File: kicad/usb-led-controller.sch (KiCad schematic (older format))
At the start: 45 parts, among them J1 SWD, J2 PWR, J3 USB, J4 PWM_0, J5 PWM_1, J6 WS2812_0, J7 WS2812_1, Q1 NVS4409N, Q2 NVS4409N, Q3 NVS4409N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

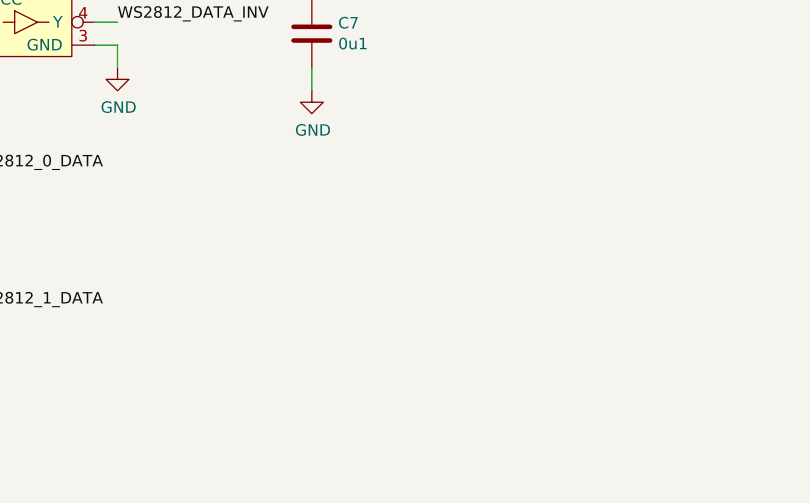
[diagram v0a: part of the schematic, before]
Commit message: Added some pullups
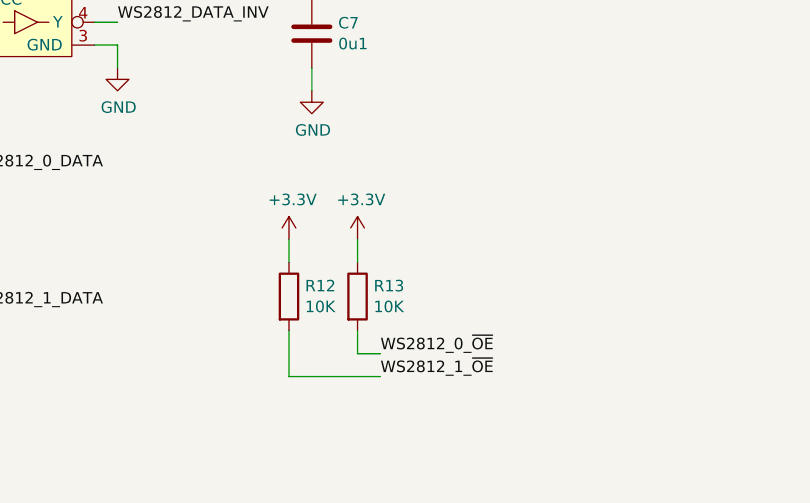
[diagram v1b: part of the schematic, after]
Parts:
- added R12, R13: 10K, Resistor_SMD:R_0402_1005Metric, symbol Device:R
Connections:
- net +3V3: now also R12.1, R13.1
- net WS2812_0_~OE: now also R13.2
- net WS2812_1_~OE: now also R12.2
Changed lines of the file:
@@
 	0    1    1    0
 $EndComp
+$Comp
+L Device:R R12
+U 1 1 5FC2AA22
+P 5950 6950
+F 0 "R12" H 6020 6996 50  0000 L CNN
+F 1 "10K" H 6020 6905 50  0000 L CNN
+F 2 "Resistor_SMD:R_0402_1005Metric" V 5880 6950 50  0001 C CNN
+F 3 "~" H 5950 6950 50  0001 C CNN
+	1    5950 6950
+	1    0    0    -1
+$EndComp
+$Comp
+L Device:R R13
+U 1 1 5FC2B0C0
+P 6250 6950
+F 0 "R13" H 6320 6996 50  0000 L CNN
+F 1 "10K" H 6320 6905 50  0000 L CNN
+F 2 "Resistor_SMD:R_0402_1005Metric" V 6180 6950 50  0001 C CNN
+F 3 "~" H 6250 6950 50  0001 C CNN
+	1    6250 6950
+	1    0    0    -1
+$EndComp
+$Comp
+L power:+3.3V #PWR02
+U 1 1 5FC2BA79
+P 5950 6700
+F 0 "#PWR02" H 5950 6550 50  0001 C CNN
+F 1 "+3.3V" H 5965 6873 50  0000 C CNN
+F 2 "" H 5950 6700 50  0001 C CNN
+F 3 "" H 5950 6700 50  0001 C CNN
+	1    5950 6700
+	1    0    0    -1
+$EndComp
+$Comp
+L power:+3.3V #PWR03
+U 1 1 5FC2C655
+P 6250 6700
+F 0 "#PWR03" H 6250 6550 50  0001 C CNN
+F 1 "+3.3V" H 6265 6873 50  0000 C CNN
+F 2 "" H 6250 6700 50  0001 C CNN
+F 3 "" H 6250 6700 50  0001 C CNN
+	1    6250 6700
+	1    0    0    -1
+$EndComp
+Text Label 6350 7200 0    50   ~ 0
+WS2812_0_~OE
+Wire Wire Line
+	6350 7200 6250 7200
+Wire Wire Line
+	6250 7200 6250 7100
+Text Label 6350 7300 0    50   ~ 0
+WS2812_1_~OE
+Wire Wire Line
+	6350 7300 5950 7300
+Wire Wire Line
+	5950 7300 5950 7100
+Wire Wire Line
+	5950 6800 5950 6700
+Wire Wire Line
+	6250 6700 6250 6800
 $EndSCHEMATC

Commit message: Updated part numbers on schematic for building
This doesn't belong on this branch..
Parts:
- J1: Part Number (none) -> 455-1790-1-ND
- J2: Part Number (none) -> 952-3233-ND
- J6, J7: Part Number (none) -> 952-3232-ND
- R1, R3, R5: Part Number (none) -> CR0402-J/-000GLFTR-ND
- R10, R11, R12, R13: Part Number (none) -> CR0402-JW-103GLFTR-ND
- R2: Part Number (none) -> CR0402-FX-1001GLFTR-ND
- R6, R7, R8, R9: Part Number (none) -> CR0402-JW-330GLFTR-ND
- U6: Part Number (none) -> 296-11600-2-ND
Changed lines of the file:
@@
 F 1 "SWD" H 718 2566 50  0000 C CNN
 F 2 "usb-led-controller:JST-SH-4" H 800 2900 50  0001 C CNN
-F 3 "455-1790-1-ND" H 800 2900 50  0001 C CNN
+F 3 "~" H 800 2900 50  0001 C CNN
+F 4 "455-1790-1-ND" H 800 2900 50  0001 C CNN "Part Number"
 	1    800  2900
 	-1   0    0    1
@@
 F 2 "Resistor_SMD:R_0402_1005Metric" V 4530 4450 50  0001 C CNN
 F 3 "~" H 4600 4450 50  0001 C CNN
+F 4 "CR0402-JW-330GLFTR-ND" H 4600 4450 50  0001 C CNN "Part Number"
 	1    4600 4450
 	0    1    1    0
@@
 F 2 "Resistor_SMD:R_0402_1005Metric" V 4530 4750 50  0001 C CNN
 F 3 "~" H 4600 4750 50  0001 C CNN
+F 4 "CR0402-JW-330GLFTR-ND" H 4600 4750 50  0001 C CNN "Part Number"
 	1    4600 4750
 	0    1    1    0
@@
 F 2 "Resistor_SMD:R_0402_1005Metric" V 3580 1200 50  0001 C CNN
 F 3 "~" H 3650 1200 50  0001 C CNN
+F 4 "CR0402-FX-1001GLFTR-ND" H 3650 1200 50  0001 C CNN "Part Number"
 	1    3650 1200
 	1    0    0    -1
@@
 F 2 "Resistor_SMD:R_0402_1005Metric" V 4180 1150 50  0001 C CNN
 F 3 "~" H 4250 1150 50  0001 C CNN
+F 4 "CR0402-J/-000GLFTR-ND" H 4250 1150 50  0001 C CNN "Part Number"
 	1    4250 1150
 	0    1    1    0
@@
 F 2 "Resistor_SMD:R_0402_1005Metric" V 730 3700 50  0001 C CNN
 F 3 "~" H 800 3700 50  0001 C CNN
+F 4 "CR0402-J/-000GLFTR-ND" H 800 3700 50  0001 C CNN "Part Number"
 	1    800  3700
 	1    0    0    -1
@@
 F 2 "usb-led-controller:M20-88904" H 800 5300 50  0001 C CNN
 F 3 "~" H 800 5300 50  0001 C CNN
+F 4 "952-3233-ND" H 800 5300 50  0001 C CNN "Part Number"
 	1    800  5300
 	-1   0    0    -1
@@
 F 2 "usb-led-controller:M20-88903" H 10450 2950 50  0001 C CNN
 F 3 "~" H 10450 2950 50  0001 C CNN
+F 4 "952-3232-ND" H 10450 2950 50  0001 C CNN "Part Number"
 	1    10450 2950
 	1    0    0    -1
@@
 F 2 "Resistor_SMD:R_0402_1005Metric" V 3730 6400 50  0001 C CNN
 F 3 "~" H 3800 6400 50  0001 C CNN
+F 4 "CR0402-JW-330GLFTR-ND" H 3800 6400 50  0001 C CNN "Part Number"
 	1    3800 6400
 	0    1    1    0
@@
 F 2 "Resistor_SMD:R_0402_1005Metric" V 3730 7000 50  0001 C CNN
 F 3 "~" H 3800 7000 50  0001 C CNN
+F 4 "CR0402-JW-330GLFTR-ND" H 3800 7000 50  0001 C CNN "Part Number"
 	1    3800 7000
 	0    1    1    0
@@
 F 2 "Resistor_SMD:R_0402_1005Metric" V 3880 5050 50  0001 C CNN
 F 3 "~" H 3950 5050 50  0001 C CNN
+F 4 "CR0402-J/-000GLFTR-ND" H 3950 5050 50  0001 C CNN "Part Number"
 	1    3950 5050
 	1    0    0    -1
@@
 F 2 "usb-led-controller:M20-88903" H 10450 3350 50  0001 C CNN
 F 3 "~" H 10450 3350 50  0001 C CNN
+F 4 "952-3232-ND" H 10450 3350 50  0001 C CNN "Part Number"
 	1    10450 3350
 	1    0    0    -1
@@
 F 2 "Package_TO_SOT_SMD:SOT-353_SC-70-5" H 4800 5750 50  0001 C CNN
 F 3 "" H 4800 5750 50  0001 C CNN
+F 4 "296-11600-2-ND" H 4800 5750 50  0001 C CNN "Part Number"
 	1    4800 5750
 	1    0    0    -1
@@
 F 2 "Resistor_SMD:R_0402_1005Metric" V 4230 7300 50  0001 C CNN
 F 3 "~" H 4300 7300 50  0001 C CNN
+F 4 "CR0402-JW-103GLFTR-ND" H 4300 7300 50  0001 C CNN "Part Number"
 	1    4300 7300
 	1    0    0    -1
@@
 F 2 "Resistor_SMD:R_0402_1005Metric" V 3980 6650 50  0001 C CNN
 F 3 "~" H 4050 6650 50  0001 C CNN
+F 4 "CR0402-JW-103GLFTR-ND" H 4050 6650 50  0001 C CNN "Part Number"
 	1    4050 6650
 	1    0    0    -1
@@
 F 2 "Resistor_SMD:R_0402_1005Metric" V 5880 6950 50  0001 C CNN
 F 3 "~" H 5950 6950 50  0001 C CNN
+F 4 "CR0402-JW-103GLFTR-ND" H 5950 6950 50  0001 C CNN "Part Number"
 	1    5950 6950
 	1    0    0    -1
@@
 F 2 "Resistor_SMD:R_0402_1005Metric" V 6180 6950 50  0001 C CNN
 F 3 "~" H 6250 6950 50  0001 C CNN
+F 4 "CR0402-JW-103GLFTR-ND" H 6250 6950 50  0001 C CNN "Part Number"
 	1    6250 6950
 	1    0    0    -1

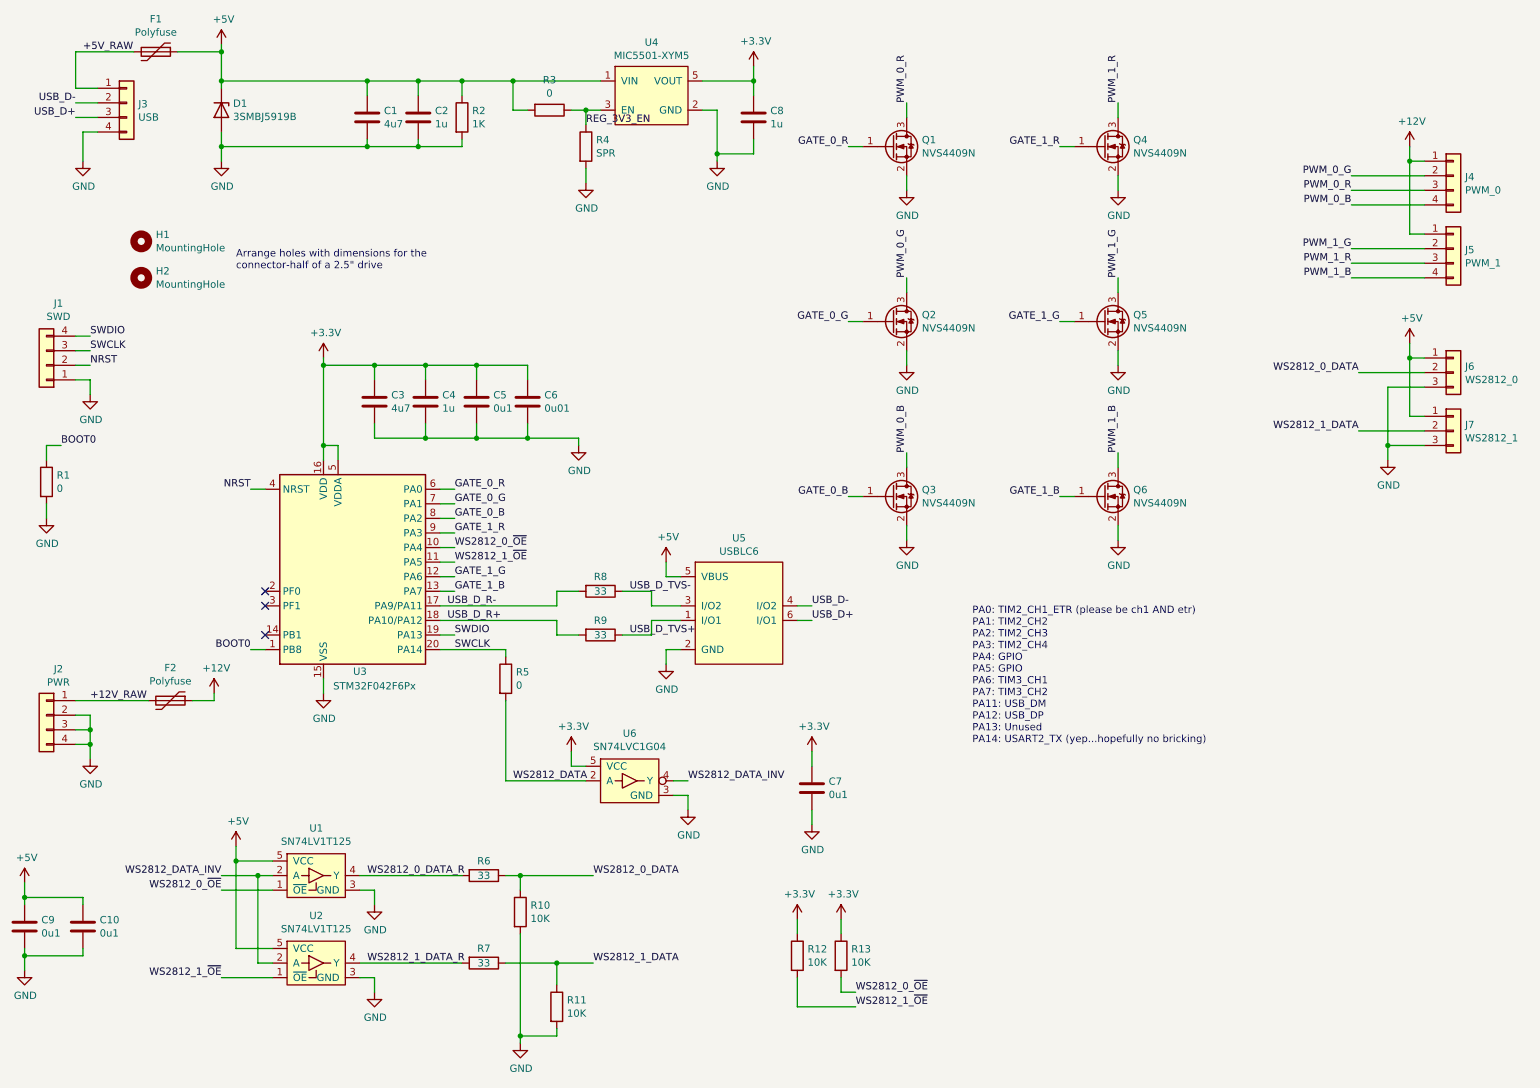
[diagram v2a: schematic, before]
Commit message: Updating schematic to use an EFM32HG microcontroller
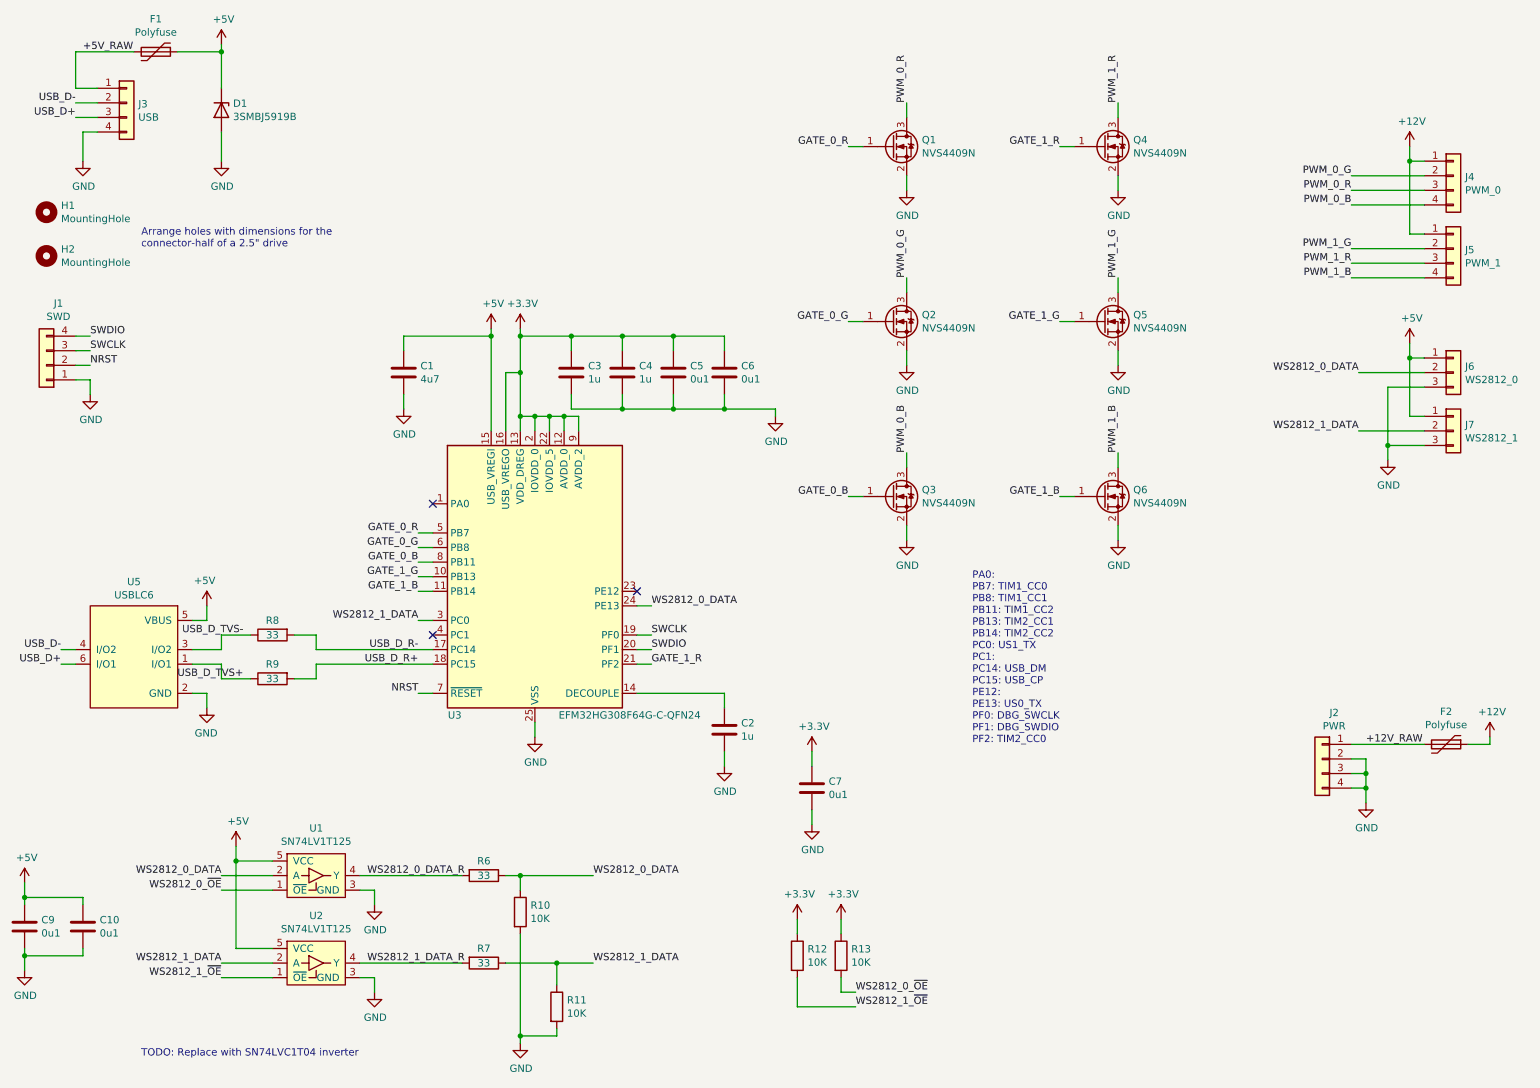
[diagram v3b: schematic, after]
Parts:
- removed C8: 1u, Capacitor_SMD:C_0603_1608Metric, symbol Device:C
- removed R1, R3, R5: 0, Resistor_SMD:R_0402_1005Metric, symbol Device:R
- removed R2: 1K, Resistor_SMD:R_0402_1005Metric, symbol Device:R
- removed R4: SPR, Resistor_SMD:R_0402_1005Metric, symbol Device:R
- removed U3: STM32F042F6Px, Package_SO:TSSOP-20_4.4x6.5mm_P0.65mm, symbol MCU_ST_STM32F0:STM32F042F6Px
- removed U4: MIC5501-XYM5, Package_TO_SOT_SMD:SOT-23-5, symbol usb-led-controller:MIC5501-XYM5
- removed U6: SN74LVC1G04, Package_TO_SOT_SMD:SOT-353_SC-70-5, symbol usb-led-controller:SN74LVC1G04
- added U3: EFM32HG308F64G-C-QFN24, Package_DFN_QFN:QFN-24-1EP_5x5mm_P0.65mm_EP3.6x3.6mm, symbol MCU_SiliconLabs:EFM32HG308F64G-C-QFN24
- C3: value 4u7 -> 1u; Part Number 1276-1044-2-ND -> 1276-1102-2-ND
- C6: value 0u01 -> 0u1; Part Number 587-5482-2-ND -> 1276-1043-2-ND
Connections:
- net +3V3: now also U3.12 (AVDD_0), U3.13 (VDD_DREG), U3.16 (USB_VREGO), U3.2 (IOVDD_0), U3.22 (IOVDD_5), U3.9 (AVDD_2)
- net +5V: now also U3.15 (USB_VREGI); no longer C2.1
- net GATE_0_B: now also U3.8 (PB11)
- net GATE_0_G: now also U3.6 (PB8)
- net GATE_0_R: now also U3.5 (PB7)
- net GATE_1_B: now also U3.11 (PB14)
- net GATE_1_G: now also U3.10 (PB13)
- net GATE_1_R: now also U3.21 (PF2)
- net GND: now also U3.25 (VSS)
- net NRST: now also U3.7 (~RESET)
- net SWCLK: now also U3.19 (PF0)
- net SWDIO: now also U3.20 (PF1)
- net USB_D_R+: now also U3.18 (PC15)
- net USB_D_R-: now also U3.17 (PC14)
- net WS2812_0_DATA: now also U1.2 (A), U3.24 (PE13)
- net WS2812_1_DATA: now also U2.2 (A), U3.3 (PC0)
- removed net WS2812_DATA_INV: U1.2 (A), U2.2 (A)
- new net: C2.1, U3.14 (DECOUPLE)
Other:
- note added: "PA0:\nPB7: TIM1_CC0\nPB8: TIM1_CC1\nPB11: TIM1_CC2\nPB13: TIM2_CC1\nPB14: TIM2_CC2\nPC0: US1_TX\nPC1:\nPC14: USB_DM\nPC15: USB_CP\nPE12:\nPE13: US0_TX\nPF0: DBG_SWCLK\nPF1: DBG_SWDIO\nPF2: TIM2_CC0"
- note added: "TODO: Replace with SN74LVC1T04 inverter"
- note removed: "PA0: TIM2_CH1_ETR (please be ch1 AND etr)\nPA1: TIM2_CH2\nPA2: TIM2_CH3\nPA3: TIM2_CH4\nPA4: GPIO\nPA5: GPIO\nPA6: TIM3_CH1\nPA7: TIM3_CH2\nPA11: USB_DM\nPA12: USB_DP\nPA13: Unused\nPA14: USART2_TX (yep...hopefully no bricking)"
- moved on the sheet: C1, C3, C4, C5, C6, F2, H1, H2, J2, R8, R9, U5

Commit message: Placed new microcontroller and rearranged capacitors
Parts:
- removed C7: 0u1, Capacitor_SMD:C_0402_1005Metric, symbol Device:C
- C4: value 1u -> 0u1; footprint Capacitor_SMD:C_0603_1608Metric -> Capacitor_SMD:C_0402_1005Metric; Part Number 1276-1102-2-ND -> 1276-1043-2-ND
- U3: footprint Package_DFN_QFN:QFN-24-1EP_5x5mm_P0.65mm_EP3.6x3.6mm -> Package_DFN_QFN:QFN-24-1EP_5x5mm_P0.65mm_EP3.6x3.6mm_ThermalVias
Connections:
- net WS2812_0_DATA: no longer U1.2 (A), U3.24 (PE13)
- net WS2812_0_~OE: now also U3.23 (PE12)
- net WS2812_1_DATA: no longer U2.2 (A), U3.3 (PC0)
- net WS2812_1_~OE: now also U3.4 (PC1)
- net UC_DECOUPLE: now reaches C2.1, U3.14 (DECOUPLE)
- new net WS2812_0_DATA_UC: U1.2 (A), U3.24 (PE13)
- new net WS2812_1_DATA_UC: U2.2 (A), U3.3 (PC0)
- no-connect marks 3 -> 1
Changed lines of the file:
@@
 P 4750 2950
 F 0 "C4" H 4865 2996 50  0000 L CNN
-F 1 "1u" H 4865 2905 50  0000 L CNN
-F 2 "Capacitor_SMD:C_0603_1608Metric" H 4788 2800 50  0001 C CNN
+F 1 "0u1" H 4865 2905 50  0000 L CNN
+F 2 "Capacitor_SMD:C_0402_1005Metric" H 4788 2800 50  0001 C CNN
 F 3 "~" H 4750 2950 50  0001 C CNN
-F 4 "1276-1102-2-ND" H 4750 2950 50  0001 C CNN "Part Number"
+F 4 "1276-1043-2-ND" H 4750 2950 50  0001 C CNN "Part Number"
 	1    4750 2950
 	1    0    0    -1
@@
 F 4 "1276-1043-2-ND" H 5450 2950 50  0001 C CNN "Part Number"
 	1    5450 2950
-	1    0    0    -1
-$EndComp
-$Comp
-L Device:C C7
-U 1 1 5FC0A218
-P 6050 5800
-F 0 "C7" H 6165 5846 50  0000 L CNN
-F 1 "0u1" H 6165 5755 50  0000 L CNN
-F 2 "Capacitor_SMD:C_0402_1005Metric" H 6088 5650 50  0001 C CNN
-F 3 "~" H 6050 5800 50  0001 C CNN
-F 4 "1276-1043-2-ND" H 6050 5800 50  0001 C CNN "Part Number"
-	1    6050 5800
 	1    0    0    -1
 $EndComp
@@
 	2950 6400 3650 6400
 Text Label 2000 6400 2    50   ~ 0
-WS2812_0_DATA
+WS2812_0_DATA_UC
 $Comp
 L Connector_Generic:Conn_01x04 J3
@@
 Wire Wire Line
 	650  6950 650  7050
-$Comp
-L power:+3.3V #PWR0133
-U 1 1 5FD00D52
-P 6050 5550
-F 0 "#PWR0133" H 6050 5400 50  0001 C CNN
-F 1 "+3.3V" H 6065 5723 50  0000 C CNN
-F 2 "" H 6050 5550 50  0001 C CNN
-F 3 "" H 6050 5550 50  0001 C CNN
-	1    6050 5550
-	1    0    0    -1
-$EndComp
-Wire Wire Line
-	6050 5550 6050 5650
-$Comp
-L power:GND #PWR0134
-U 1 1 5FD0A22D
-P 6050 6050
-F 0 "#PWR0134" H 6050 5800 50  0001 C CNN
-F 1 "GND" H 6055 5877 50  0000 C CNN
-F 2 "" H 6050 6050 50  0001 C CNN
-F 3 "" H 6050 6050 50  0001 C CNN
-	1    6050 6050
-	1    0    0    -1
-$EndComp
-Wire Wire Line
-	6050 6050 6050 5950
 $Comp
 L Device:R R11
@@
 F 0 "U3" H 3600 3400 50  0000 C CNN
 F 1 "EFM32HG308F64G-C-QFN24" H 4800 3400 50  0000 C CNN
-F 2 "Package_DFN_QFN:QFN-24-1EP_5x5mm_P0.65mm_EP3.6x3.6mm" H 4200 3400 50  0001 C CNN
+F 2 "Package_DFN_QFN:QFN-24-1EP_5x5mm_P0.65mm_EP3.6x3.6mm_ThermalVias" H 4200 3400 50  0001 C CNN
 F 3 "https://www.silabs.com/documents/public/data-sheets/efm32hg-datasheet.pdf" H 4200 3400 50  0001 C CNN
 	1    4150 4350
@@
 	2000 6400 2350 6400
 Text Label 2000 7000 2    50   ~ 0
-WS2812_1_DATA
+WS2812_1_DATA_UC
 Wire Wire Line
 	2000 7000 2350 7000
@@
 TODO: Replace with SN74LVC1T04 inverter
 Text Label 4950 4550 0    50   ~ 0
-WS2812_0_DATA
+WS2812_0_DATA_UC
 Text Label 3350 4650 2    50   ~ 0
-WS2812_1_DATA
+WS2812_1_DATA_UC
 Wire Wire Line
 	3450 4650 3350 4650
@@
 Wire Wire Line
 	3350 4250 3450 4250
-NoConn ~ 3450 4750
-NoConn ~ 4850 4450
 Text Label 4950 4950 0    50   ~ 0
 GATE_1_R
@@
 Wire Wire Line
 	2000 1300 2000 1500
+Text Label 4950 4450 0    50   ~ 0
+WS2812_0_~OE
+Text Label 3350 4750 2    50   ~ 0
+WS2812_1_~OE
+Wire Wire Line
+	4950 4450 4850 4450
+Wire Wire Line
+	3450 4750 3350 4750
+Text Label 4950 5150 0    50   ~ 0
+UC_DECOUPLE
 $EndSCHEMATC
